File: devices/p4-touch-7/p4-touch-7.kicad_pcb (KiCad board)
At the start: 4 copper layers, 160 x 96 mm, 229 parts, among them J1 USB4105-GF-A, J2 USB4105-GF-A, J3 USB4105-GF-A, J4 MX1.25-2P, J5 DM3AT-SF-PEJM5, Q1 MMBT3904-7-F, Q2 MMBT3904-7-F, SW1 PTS810SJM250SMTR LFS, SW2 PTS810SJM250SMTR LFS, SW3 PTS645SM43SMTR92 LFS, U1 ESP32-P4NRW32, U10 DS3231SN#, U11 ESP32-C6-MINI-1-N4, U12 USBLC6-2SC6, U13 W25Q128JVSIQ, U14 USBLC6-2SC6, U15 USBLC6-2SC6, U2 IP5306, U3 SY8089AAAC, U4 SY8089AAAC, U5 CH340C, U6 MT3608, U7 MT3608, U8 ES8311, U9 PAM8403DR, Y1 40MHz 10pF

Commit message: devices: p4-touch-7 with its parts' LCSC codes: the fabrication files export
Claude-Session: https://claude.ai/code/session_01GffCzZXi9ShujPbky1eccg
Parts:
- removed the LCD1 at (100.0, 200.0) (x4)
- removed the LCD1 at (180.0, 152.0) (x48)
- removed the LCD1 at (175.0, 157.0) (x4)
- added LCD1 (x4): touch-display, JC1060M070N-I, B.Cu at (100.0, 200.0)
- added LCD1 (x105): touch-display, JC1060M070N-I, B.Cu at (180.0, 152.0)
- added LCD1 (x4): touch-display, JC1060M070N-I, B.Cu at (175.0, 157.0)

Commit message: p4-touch-7, blinker, led-bar: parts chosen from JLCPCB's catalogue, the fab files export
Since the parts selection buys from JLCPCB's own catalogue, these boards' support capacitors and
connectors had no orderable part and export.run refused them. parts.select chose every group
(p4-touch-7's 40 MHz crystal pinned as on the 7B board, C426988); copper unchanged.

Claude-Session: https://claude.ai/code/session_01GffCzZXi9ShujPbky1eccg
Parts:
- removed the LCD1 at (100.0, 200.0) (x4)
- removed the LCD1 at (180.0, 152.0) (x105)
- removed the LCD1 at (175.0, 157.0) (x4)
- added LCD1 (x4): touch-display, JC1060M070N-I, B.Cu at (100.0, 200.0)
- added LCD1 (x106): touch-display, JC1060M070N-I, B.Cu at (180.0, 152.0)
- added LCD1 (x4): touch-display, JC1060M070N-I, B.Cu at (175.0, 157.0)

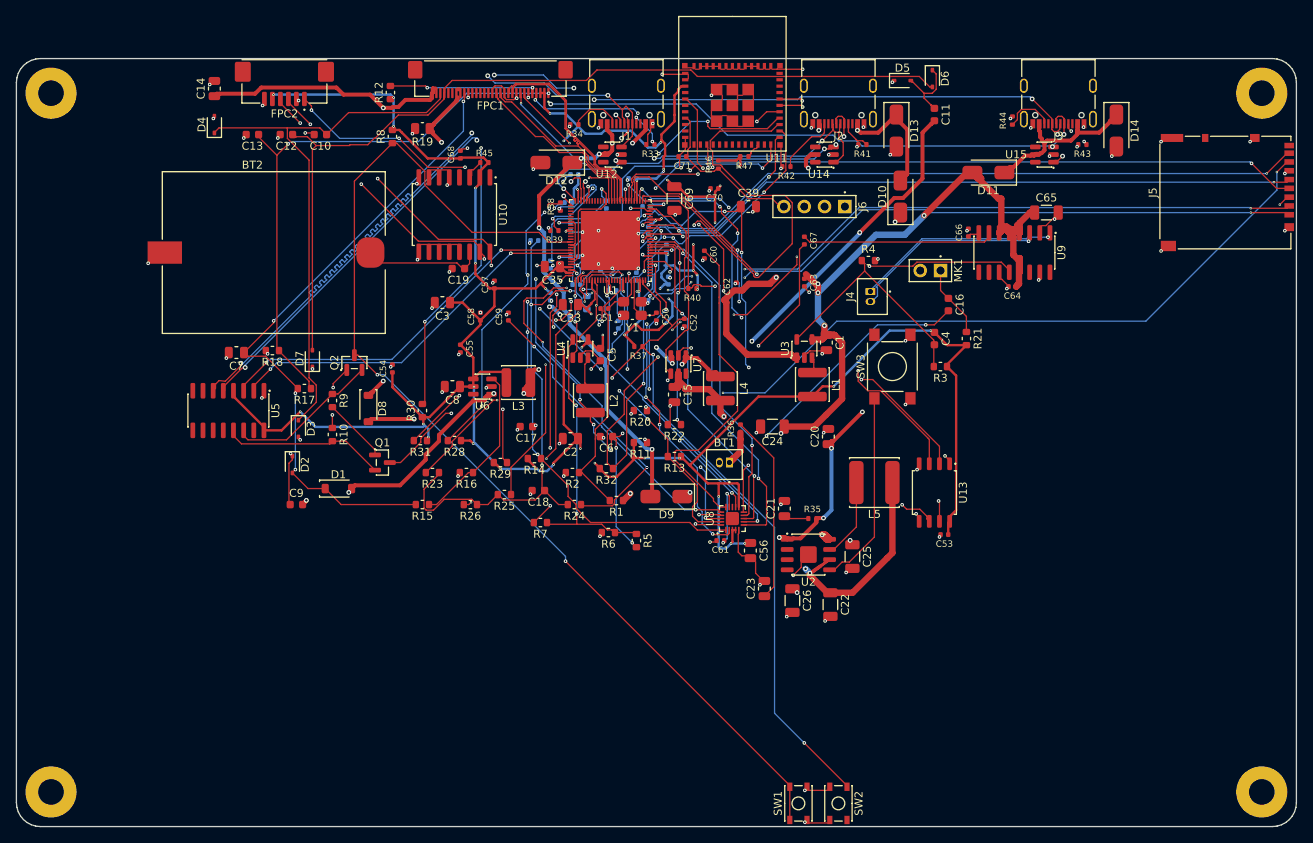
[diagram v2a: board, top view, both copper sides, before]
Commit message: Boards pass check and KiCad 10's DRC again: holes in courtyards, the USB net rename
pcbkit's check now has KiCad 10's pth/npth_inside_courtyard (pcbkit be5b6955), and 13 boards
failed it. KiCad's own DRC (kicad-cli 10) reports the same holes on every one of them.

- Parts that really stand above the holes under them (a screen or a Nano on its sockets, the
  Delta-S02's КМ-6 capacitors flat under its chips, as the factory placed them): a courtyard rule
  for the pair, written to each board's .kicad_dru, so KiCad's DRC agrees.
- Real collisions moved: servo-controller's dial 3 mm up (the Nano's socket pins came out under
  it), c3-pocket's fourth M3 hole from under a cell holder to the top edge's middle, s3-rgb's
  D-pad 2 mm up (a holder's peg came through under the down key).
- v003-emu, c3-pocket, rp2040-tft, rp2350-psram, s3-rgb, teensy41: re-routed for the standard USB
  block's renamed net (usb/raw is usb/vbusIn since pcbkit 2088839e): their tracks still carried
  the old name and shorted the fuse and connector pads.
- p4-touch-7: its board file still had a courtyard for the panel the design gives none (KiCad
  reported 114 courtyard errors); written again.

Measured on the dev host: all 44 registry boards `pcbkit check` complete with 0 errors, and
kicad-cli pcb drc 0 errors on every board.

Claude-Session: https://claude.ai/code/session_018URVYF1YPgyrMNetY9yT1T
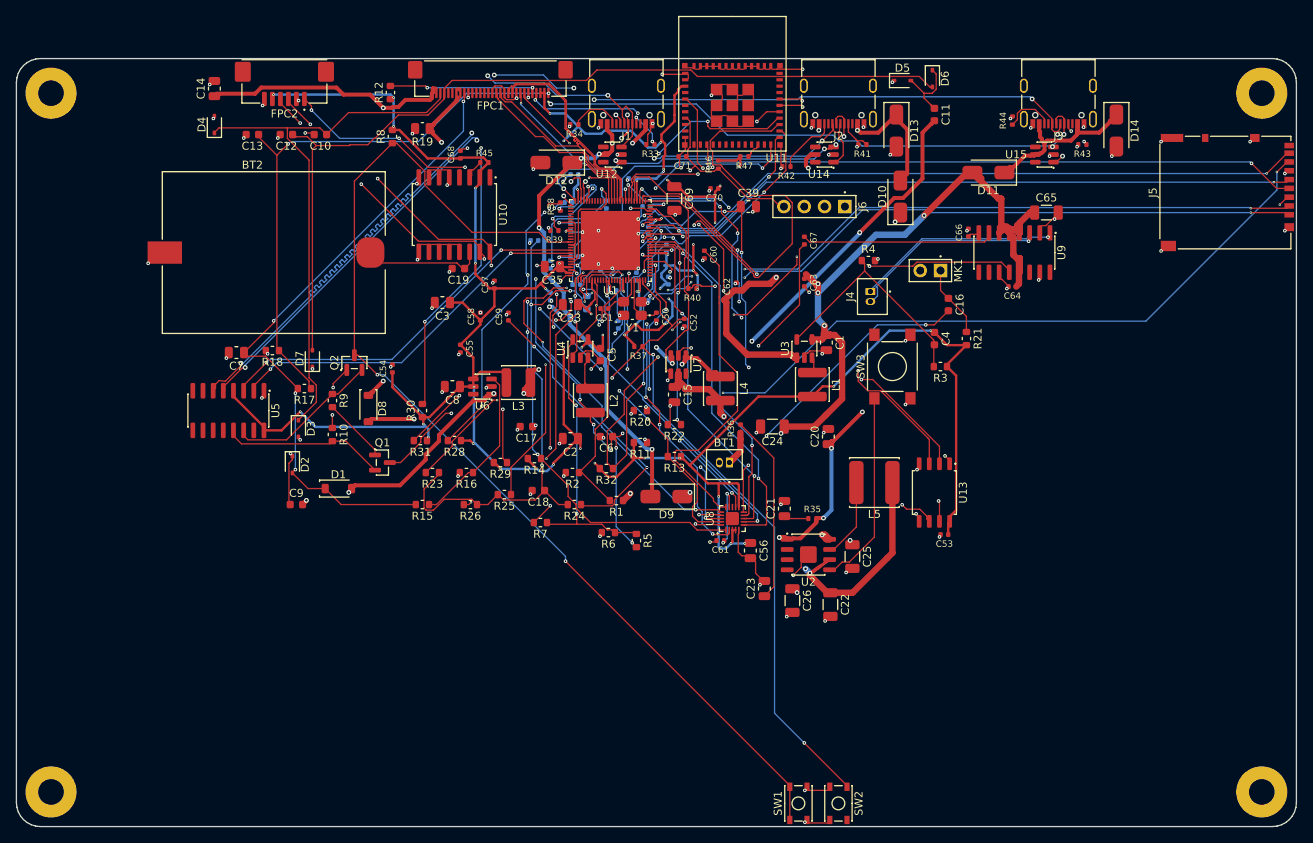
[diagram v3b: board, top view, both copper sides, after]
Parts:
- removed the LCD1 at (100.0, 200.0) (x4)
- removed the LCD1 at (180.0, 152.0) (x106)
- removed the LCD1 at (175.0, 157.0) (x4)
- added LCD1: touch-display, JC1060M070N-I, B.Cu at (180.0, 152.0)
- H1, H2, H3, H4: value (none) -> MountingHole_3.2mm_M3_Pad
- J6: value (none) -> PinHeader_1x04_P2.54mm_Vertical
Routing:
- net VSYS: track 199.1 -> 169.6 mm
- net VBUS_FS: track 41.6 -> 31.1 mm
- net VHP: track 128.9 -> 123.3 mm
- net RTC_BAT: track 18.6 -> 15.0 mm
- net VGL: track 115.7 -> 112.6 mm
- net VHP_FB: track 38.5 -> 36.0 mm
- net Net-(C43-1): track 22.6 -> 20.4 mm
- net AVDD: track 82.5 -> 80.4 mm
- net LCD_STBY: track 21.2 -> 19.2 mm
- net CHIP_PU: track 120.1 -> 118.2 mm
- net PUMP_L: track 11.7 -> 10.1 mm
- net VBAT: track 68.3 -> 66.7 mm
- net V3_FB: track 31.4 -> 29.8 mm
- net J3/power/cc2: track 7.62 -> 6.36 mm
- net J3/power/cc1: track 4.84 -> 3.71 mm
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- added copper zone on In4.Cu, net GND
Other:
- copper layers 4 -> 6

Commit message: devices/p4-touch-7: an overvoltage clamp on the backlight boost
The backlight's MT3608 regulated the LED current on FB = LEDK with nothing bounding its output.
With the panel unplugged (FPC1) the output climbs past the 30 V the switch pin takes
(intent-open-load, an error). FB now takes BL_FB through R48 (1 kΩ), and an 18 V zener (D15) from
LEDA into it holds the output near 19 V with no panel. The panel's 3S9P strings (about 9.6 V) stay
far below it.

The routing was redone for LEDK and the DSI D0 pair (a stub of LEDK was left at the old FB pin),
and `pcbkit parts` re-chose 13 stale and 3 missing parts. Check: complete, 0 errors (was 2),
25 warnings (pairs' coupling and skew, track classes, rail names, one via the router leaves on a
single layer on DSI_D0_P). The ESP32-P4NRW32 is still out of stock at JLCPCB.

Claude-Session: https://claude.ai/code/session_01B3VRfBCg9vAvGVWujVGarr
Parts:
- added D15: zener 18V, D_SOD-323, F.Cu at (187.5, 140.0)
- added R48: 1kohm, R_0603_1608Metric, B.Cu at (181.8, 141.1)
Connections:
- SW1 pad 2: BOOT -> GND
- SW2 pad 2: CHIP_PU -> GND
- SW3 pad 2: KEY -> GND
- U7 pad 3: LEDK -> BL_FB
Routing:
- net LEDA: track 67.6 -> 175.9 mm, vias 2 -> 6
- net C6_D3: track 88.5 -> 55.7 mm
- net BL_FB: track 0.00 -> 10.7 mm, vias 0 -> 1
- net LEDK: track 53.4 -> 57.3 mm, vias 5 -> 2
- net VBAT: track 66.7 -> 63.8 mm
- net DSI_D0_P: track 19.5 -> 21.2 mm, vias 2 -> 4
- net V3: track 441.6 -> 440.7 mm
- net DSI_D0_N: track 19.3 -> 18.7 mm
- net Net-(C60-1): track 41.7 -> 41.1 mm
- net VSYS: track 169.6 -> 169.0 mm
- added copper zone on F.Cu, net VBAT
- added copper zone on F.Cu, net VSYS

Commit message: devices: the thermostat's buck takes the TVS's clamp; p4-touch-7's host port is a Type-C source
- thermostat: the LM2596S-ADJ (45 V) sat under an SMBJ36A that clamps a surge near 58 V
  (rating-clamp). It is now the standard Buck block, which picks TI's LMR38020 (80 V) for the
  34 V rail; its 10 µF input capacitor is 1210 (CGA1210X5R106K630RT, 63 V). Placed again from
  scratch: 90 x 107 -> 84 x 76 mm. Up, down and mode stay on the right edge next to the OLED.
  Parts chosen from JLCPCB's catalogue. Complete: 0 errors, 1 warning (erc-rail-name).
- p4-touch-7: the USB host port J3 was a sink block (5.1 kΩ Rd on CC) with VBUS fed from VSYS
  through a Schottky. A device sees no source there. It is now pcbkit's new UsbCHost: 56 kΩ Rp on
  both CC pins to VSYS, and VBUS through an SY6280AAC limited to 750 mA (9.1 kΩ ISET). It stays on
  with the board: NucleoOS drives no enable pin. Complete: 0 errors; the router leaves two VSYS
  stubs (track-dangling warnings).

The MCU pins' nets are unchanged on both boards.

Claude-Session: https://claude.ai/code/session_01B3VRfBCg9vAvGVWujVGarr
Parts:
- removed D11: schottky, D_SMA
- removed D14: tvs 5V, D_SMA
- removed J3: USB4105-GF-A, USB_C_Receptacle_USB2.0_16P
- removed R43, R44: 5.1kohm, R_0402_1005Metric
- added C72: 1uF, C_0603_1608Metric, F.Cu at (234.5, 116.2)
- added C73: 10uF, C_0805_2012Metric, F.Cu at (239.2, 120.0)
- added D16: tvs 5V, D_SMA, F.Cu at (221.5, 107.8)
- added J7: USB4105-GF-A, USB_C_Receptacle_USB2.0_16P, F.Cu at (230.2, 112.2)
- added R49: 56kohm, R_0402_1005Metric, B.Cu at (231.0, 112.2)
- added R50: 56kohm, R_0402_1005Metric, B.Cu at (228.5, 113.7)
- added R51: 9.1kohm, R_0402_1005Metric, F.Cu at (240.8, 111.5)
- added U16: SY6280AAC, SOT-23-5, F.Cu at (238.2, 115.2)
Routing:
- net GND: track 102.2 -> 218.5 mm, vias 122 -> 245
- net VBUS_HOST: track 21.6 -> 51.1 mm
- net VSYS: track 169.0 -> 147.4 mm
- net J3/power/cc2: track 6.36 -> 0.00 mm
- net J3/power/cc1: track 3.71 -> 0.00 mm, vias 2 -> 0
- net J3/iset: track 0.00 -> 3.15 mm
- net J3/cc1: track 0.00 -> 0.52 mm, vias 0 -> 1
- net J3/cc2: track 0.00 -> 0.51 mm, vias 0 -> 1
- net DSI_D0_P: track 21.2 -> 21.5 mm, vias 4 -> 5

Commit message: registry: every board rebuilt with pcbkit main 4684674e6 - the bought part named on the board
pcbkit dc07fdfd6 writes the bought row's MPN and Manufacturer (the design's own kept as DesignMPN /
DesignManufacturer) and the build chooses parts before it places (6361ec104). Each of the 44 boards
was rebuilt (; the two P4 boards  only: their builds reroute pairs):
copper unchanged on all 44 (segments, arcs and vias counted before and after), placement kept; the
Arduino and lab boards now carry the parts the catalogue gives them. The check gains only the new
judgements: part-maker (a part bought from another maker) and part-missing on hand-fitted modules
(DS1 sockets); p4-touch-7 loses part-stale. The P4 boards keep their hole-clearance errors (a
reroute is Team 3's).

Claude-Session: https://claude.ai/code/session_01BAgp959tApA8aEg85EYgfb
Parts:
- R7: value 0mohm -> 0uohm
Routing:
- added copper zone on B.Cu, net VSYS
